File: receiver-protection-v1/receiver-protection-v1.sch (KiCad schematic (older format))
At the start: 13 parts, among them J1 INPUT, J2 OUTPUT, J3 POWER/CTRL, K1 DS1E-M-DC12V, Q1 2N3904

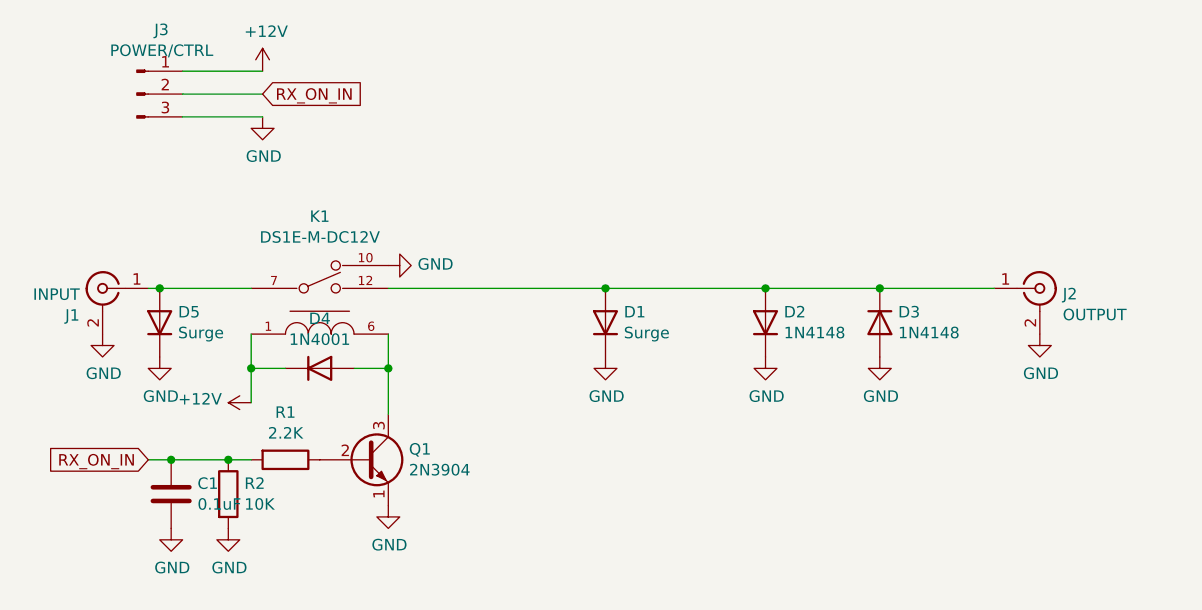
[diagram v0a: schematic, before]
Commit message: add revision 1.1 changes
* make sure the mounting hole vias are attached to ground!
* reverse input/output - make sure that the SDR facing output
  has the protection diodes and optional surge protector, and
  is grounded when the enable signal isn't applied
* label input, output, power/ground/enable
* add description, my name, and revision number
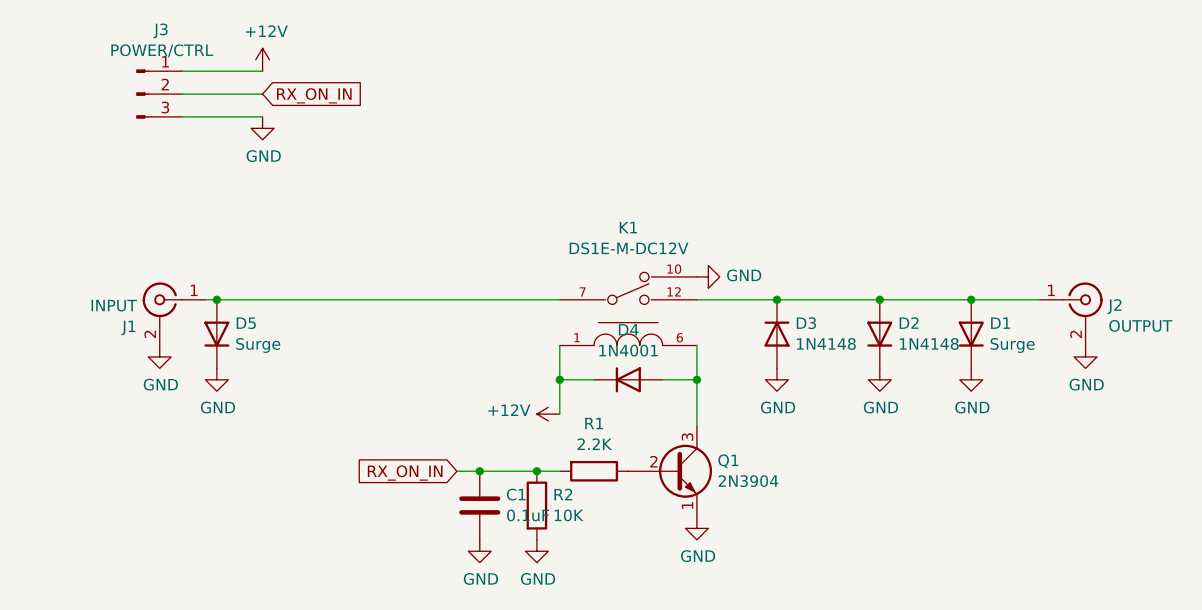
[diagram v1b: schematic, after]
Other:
- moved on the sheet: C1, D1, D2, D3, D4, D5, J1, J2, K1, Q1, R1, R2
